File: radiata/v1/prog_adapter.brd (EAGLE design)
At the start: 43.2 x 37.4 mm, 7 parts, among them J1 AVR_SPI_PRG_6

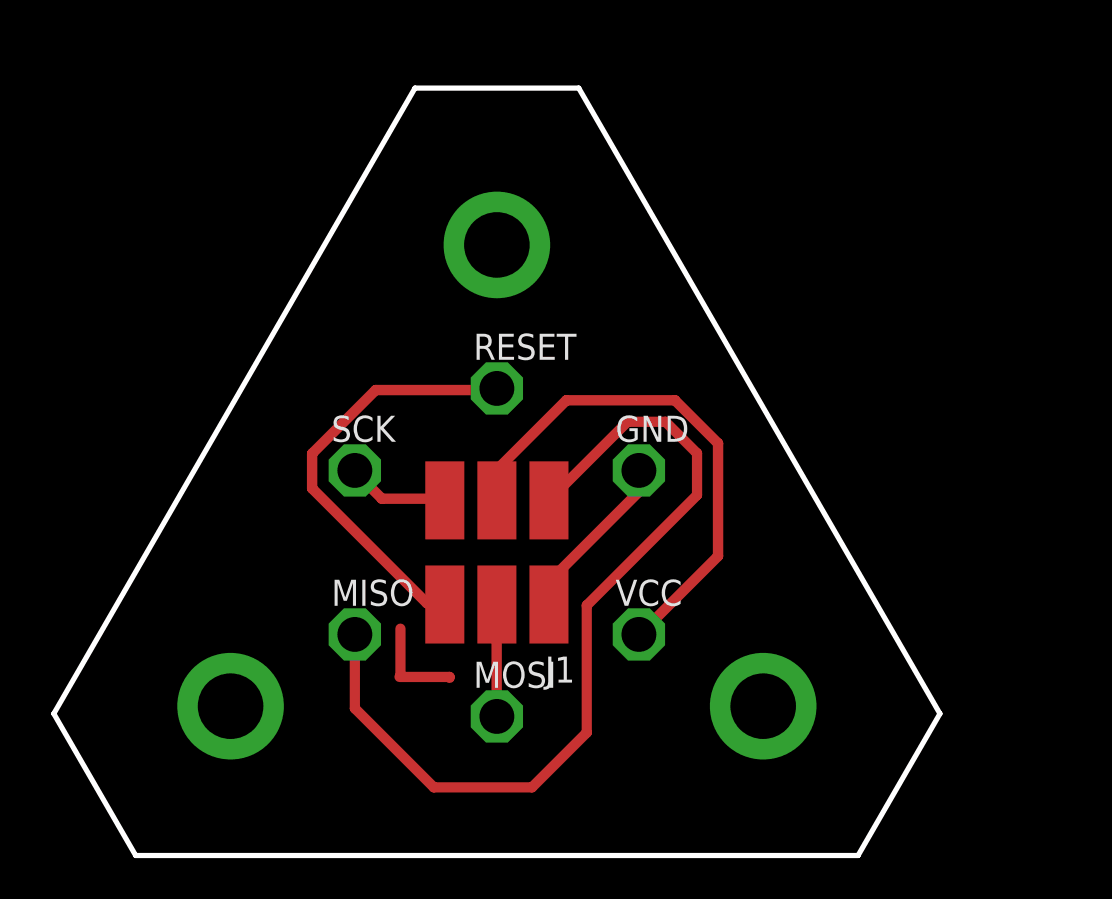
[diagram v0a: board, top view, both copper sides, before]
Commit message: fix the firmware to actually keep decent time; tested-working version of the programming remote
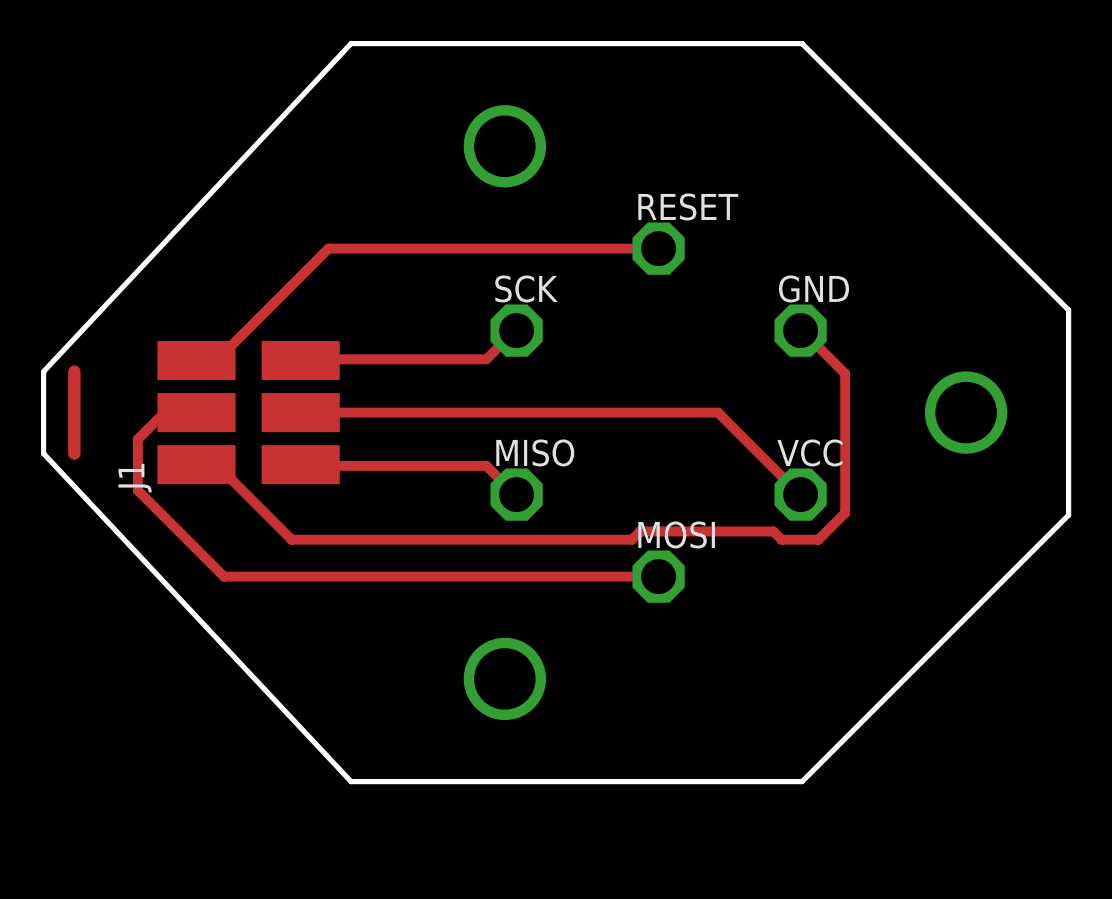
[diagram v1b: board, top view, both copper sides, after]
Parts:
- moved J1 13.9 mm to (10.0, 20.0), turned to 90 degrees
- moved GND 10.4 mm to (36.9, 24.0)
- moved VCC 10.4 mm to (36.9, 16.0)
- moved SCK 10.4 mm to (23.1, 24.0)
- moved MISO 10.4 mm to (23.1, 16.0)
- moved MOSI 10.4 mm to (30.0, 12.0)
- moved RESET 10.4 mm to (30.0, 28.0)
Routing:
- net N$6: track 8.35 -> 43.9 mm
- net N$1: track 42.9 -> 11.1 mm
- net N$5: track 5.46 -> 33.0 mm
- net N$2: track 5.03 -> 11.1 mm
- net N$12: track 0.00 -> 4.00 mm
- net N$3: track 20.9 -> 24.8 mm
- net N$11: track 2.49 -> 0.00 mm
- net N$10: track 2.26 -> 0.00 mm
- net N$4: track 25.5 -> 26.0 mm
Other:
- board size 43.2 x 37.4 mm -> 50 x 36 mm
